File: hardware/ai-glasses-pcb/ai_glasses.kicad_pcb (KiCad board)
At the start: 4 copper layers, 116 x 22 mm, 55 parts, among them J1 USB-C, J2 CAMERA DVP, J3 LiPo 1S, Q1 DMG3415U, SW1 BOOT, SW2 RESET, U1 ESP32-S3-WROOM-1-N16R8, U2 MCP73831-2-OT, U3 AP2112K-3.3, U4 TLV70028DDCR, U5 TLV70012DDCR, U6 ICS-43434, U7 MAX98357A, U8 USBLC6-2SC6

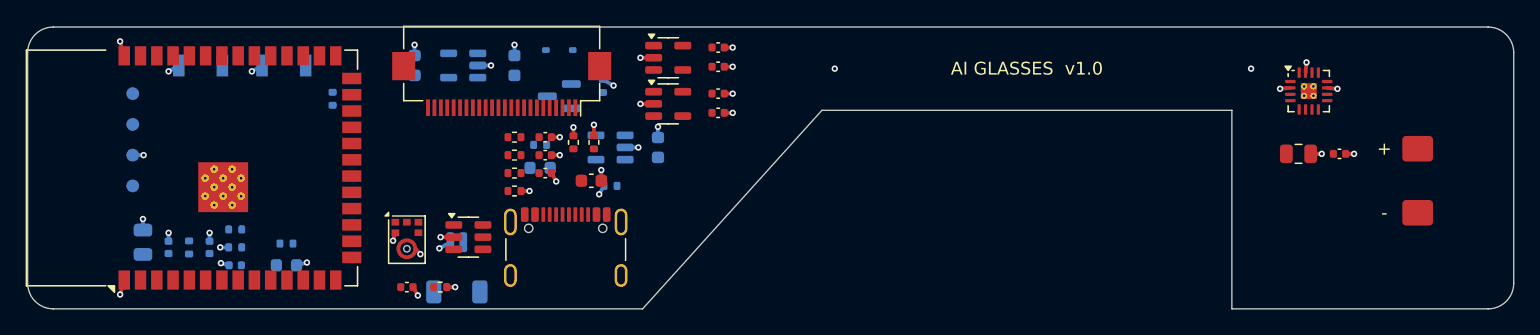
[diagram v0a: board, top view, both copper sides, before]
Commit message: AI glasses PCB: anthropometric outline, placement fixes, schematic layout
Co-Authored-By: Claude Opus 5.5 <noreply@anthropic.com>
Claude-Session: https://claude.ai/code/session_018PJ1sVCZoxAbR5ac4Gx3WA
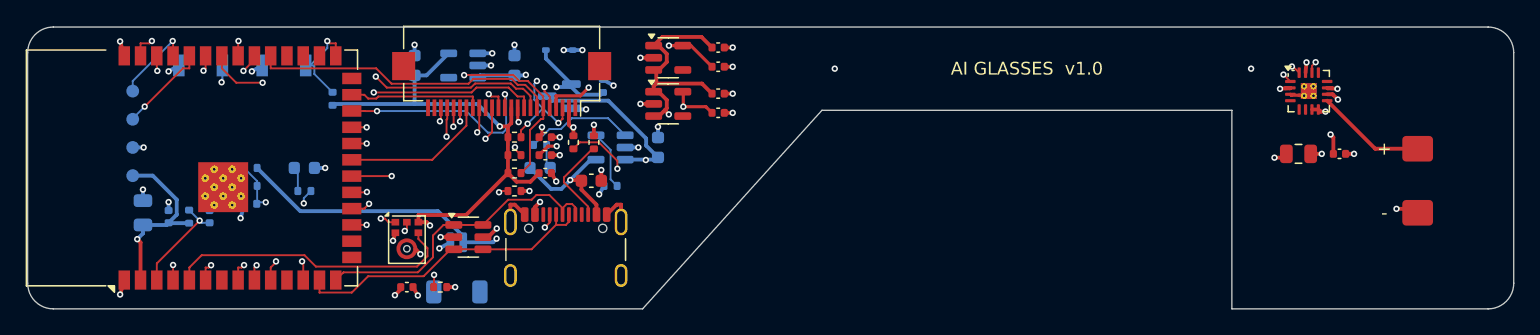
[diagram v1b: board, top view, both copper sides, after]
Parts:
- moved D3 7.73 mm to (71.6, 61.0)
- moved R10 4.95 mm to (67.4, 62.4)
- moved C15 4.95 mm to (67.4, 63.8)
- moved R9 4.95 mm to (67.4, 61.0)
- moved R8 4.33 mm to (71.6, 62.8)
- moved C13 2.40 mm to (61.0, 64.8)
- moved C14 2.40 mm to (64.2, 64.8)
- moved R6 2.40 mm to (62.6, 64.8)
- moved C12 2.30 mm to (59.0, 64.5)
- moved TP4 0.80 mm to (58.2, 61.6)
- moved TP3 0.60 mm to (58.2, 59.4)
- moved TP2 0.40 mm to (58.2, 57.2)
- moved TP1 0.20 mm to (58.2, 55.0)
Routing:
- net +3V3: track 0.00 -> 119.9 mm, vias 0 -> 5
- net AMP_BCLK: track 0.00 -> 96.4 mm, vias 0 -> 2
- net AMP_DIN: track 0.00 -> 94.0 mm, vias 0 -> 2
- net AMP_LRCLK: track 0.00 -> 94.0 mm, vias 0 -> 2
- net CAM_PWDN: track 0.00 -> 66.5 mm, vias 0 -> 3
- net VBUS: track 0.00 -> 62.9 mm, vias 0 -> 4
- net VSYS: track 32.5 -> 85.0 mm, vias 2 -> 10
- net VBAT: track 0.00 -> 49.3 mm, vias 0 -> 2
- net CAM_RESET: track 0.00 -> 41.2 mm, vias 0 -> 2
- net CAM_SIOD: track 0.00 -> 35.7 mm, vias 0 -> 4
- net CAM_SIOC: track 0.00 -> 35.7 mm, vias 0 -> 3
- net +2V8_CAM: track 0.00 -> 27.2 mm, vias 0 -> 3
- net CAM_HREF: track 0.00 -> 25.5 mm, vias 0 -> 2
- net CAM_XCLK: track 0.00 -> 24.3 mm, vias 0 -> 2
- net USB_DP: track 0.00 -> 24.2 mm
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
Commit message: AI glasses PCB: bound VSYS trunk joins, 0.127 mm default clearance
Co-Authored-By: Claude Opus 5.5 <noreply@anthropic.com>
Claude-Session: https://claude.ai/code/session_018PJ1sVCZoxAbR5ac4Gx3WA
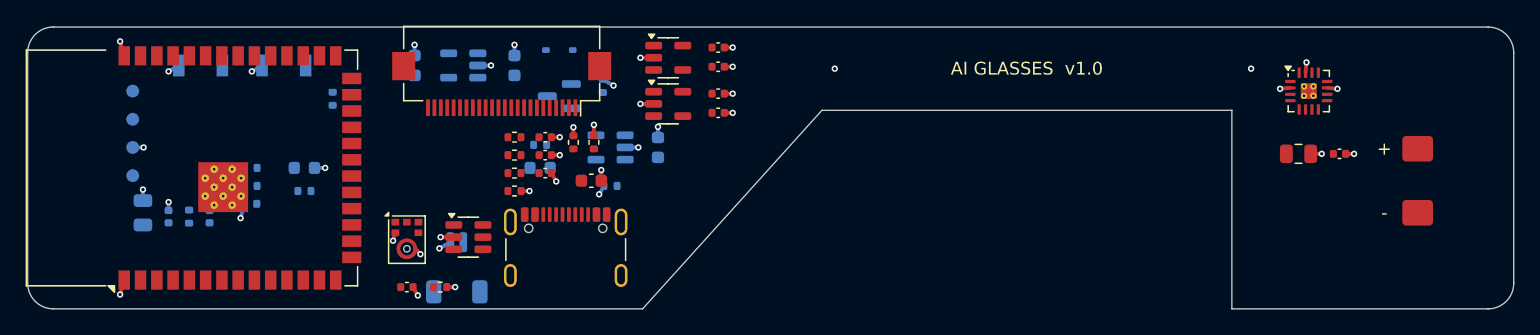
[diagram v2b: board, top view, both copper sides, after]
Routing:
- net +3V3: track 119.9 -> 0.00 mm, vias 5 -> 0
- net AMP_BCLK: track 96.4 -> 0.00 mm, vias 2 -> 0
- net AMP_DIN: track 94.0 -> 0.00 mm, vias 2 -> 0
- net AMP_LRCLK: track 94.0 -> 0.00 mm, vias 2 -> 0
- net CAM_PWDN: track 66.5 -> 0.00 mm, vias 3 -> 0
- net VBUS: track 62.9 -> 0.00 mm, vias 4 -> 0
- net VSYS: track 85.0 -> 32.5 mm, vias 10 -> 2
- net VBAT: track 49.3 -> 0.00 mm, vias 2 -> 0
- net CAM_RESET: track 41.2 -> 0.00 mm, vias 2 -> 0
- net CAM_SIOD: track 35.7 -> 0.00 mm, vias 4 -> 0
- net CAM_SIOC: track 35.7 -> 0.00 mm, vias 3 -> 0
- net +2V8_CAM: track 27.2 -> 0.00 mm, vias 3 -> 0
- net CAM_HREF: track 25.5 -> 0.00 mm, vias 2 -> 0
- net CAM_XCLK: track 24.3 -> 0.00 mm, vias 2 -> 0
- net USB_DP: track 24.2 -> 0.00 mm
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
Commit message: AI glasses PCB: stitch routed VSYS into In2 pour, tighter GND fan-out
Co-Authored-By: Claude Opus 5.5 <noreply@anthropic.com>
Claude-Session: https://claude.ai/code/session_018PJ1sVCZoxAbR5ac4Gx3WA
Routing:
- net VSYS: track 32.5 -> 0.00 mm, vias 2 -> 0

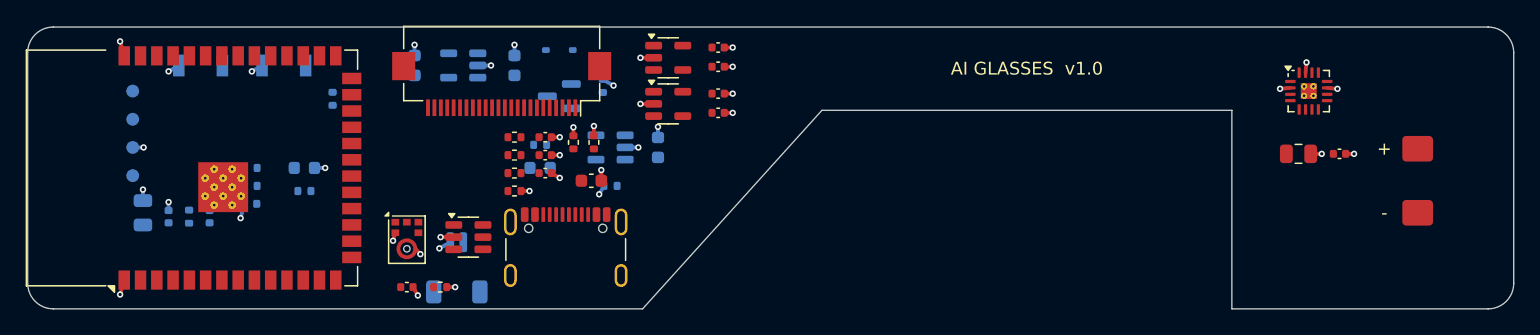
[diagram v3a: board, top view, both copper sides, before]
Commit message: AI glasses PCB: axis-aligned GND fan-out candidates, router retry strategy
Co-Authored-By: Claude Opus 5.5 <noreply@anthropic.com>
Claude-Session: https://claude.ai/code/session_018PJ1sVCZoxAbR5ac4Gx3WA
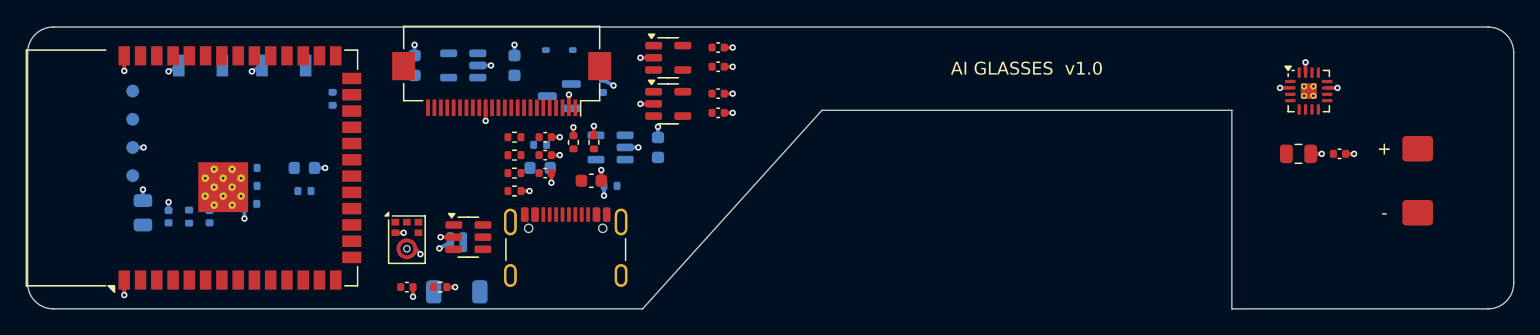
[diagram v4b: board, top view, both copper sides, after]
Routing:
- net GND: track 33.1 -> 35.2 mm, vias 40 -> 42

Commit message: AI glasses PCB: add VSYS strip pour after routing
Co-Authored-By: Claude Opus 5.5 <noreply@anthropic.com>
Claude-Session: https://claude.ai/code/session_018PJ1sVCZoxAbR5ac4Gx3WA
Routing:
- removed copper zone on In2.Cu, net VSYS

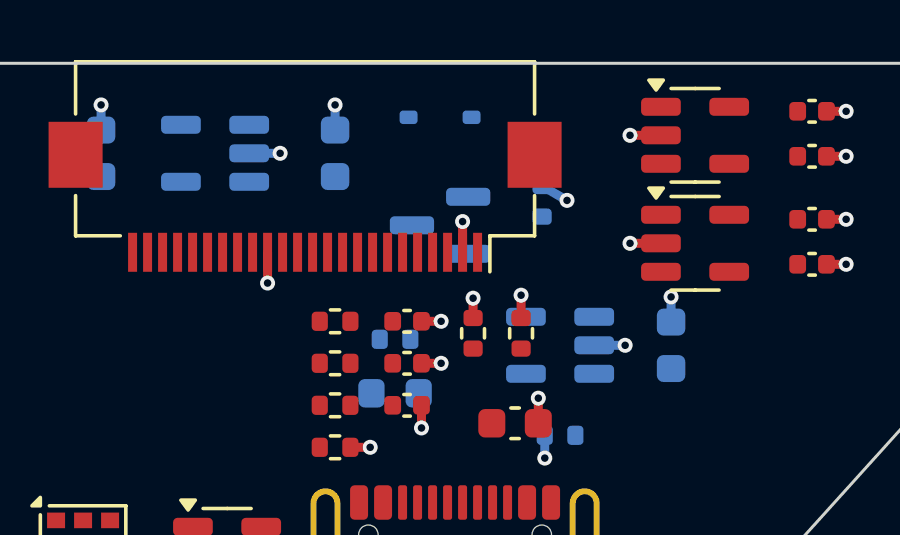
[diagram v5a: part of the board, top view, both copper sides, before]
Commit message: AI glasses PCB: reorient power-path D1/Q1 so VSYS pins are adjacent
Co-Authored-By: Claude Opus 5.5 <noreply@anthropic.com>
Claude-Session: https://claude.ai/code/session_018PJ1sVCZoxAbR5ac4Gx3WA
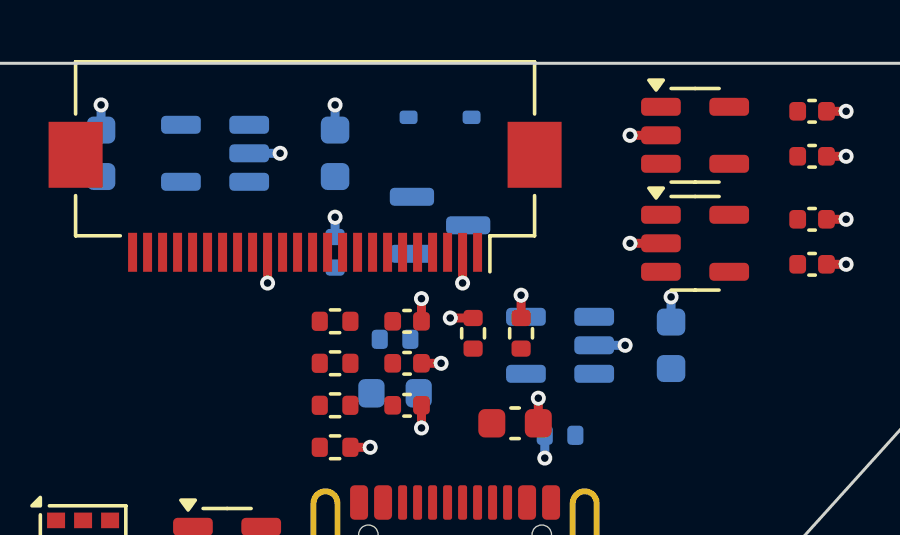
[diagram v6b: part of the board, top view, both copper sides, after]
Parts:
- moved R3 7.11 mm to (88.0, 56.3)
- turned D1 to 0 degrees
- turned Q1 to 0 degrees
